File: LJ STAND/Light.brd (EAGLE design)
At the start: 112.3 x 112.3 mm, 182 parts

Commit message: Light PCB routing
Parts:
- moved C19 4.65 mm to (55.1, 17.6), flipped to the bottom, turned to 180 degrees
- moved C17 4.47 mm to (68.4, 19.7), flipped to the bottom, turned to 160 degrees
- moved C18 4.41 mm to (61.7, 18.0), flipped to the bottom, turned to 170 degrees
- moved C21 4.19 mm to (42.3, 20.1), flipped to the bottom, turned to 200 degrees
- moved C6 4.15 mm to (94.6, 55.0), flipped to the bottom, turned to 90 degrees
- moved C13 4.12 mm to (57.3, 94.7), turned to 0 degrees
- moved C9 3.97 mm to (89.1, 36.2), flipped to the bottom, turned to 120 degrees
- moved C22 3.97 mm to (36.2, 23.2), flipped to the bottom, turned to 210 degrees
- moved C8 3.90 mm to (92.1, 42.2), flipped to the bottom, turned to 110 degrees
- moved R27 3.89 mm to (60.6, 91.9), turned to 280 degrees
- moved C20 3.89 mm to (48.6, 18.6), flipped to the bottom, turned to 190 degrees
- moved C10 3.87 mm to (85.1, 30.6), flipped to the bottom, turned to 130 degrees
- moved C14 3.86 mm to (63.8, 94.0), turned to 10 degrees
- moved C25 3.84 mm to (22.4, 37.7), flipped to the bottom, turned to 240 degrees
- moved R25 3.82 mm to (54.2, 92.1), turned to 270 degrees
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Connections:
- removed net N$43: U$1.6
- removed net N$44: U$1.5
- removed net N$45: U$1.4
- removed net N$46: U$1.3
- removed net N$47: U$1.2
- removed net N$48: U$1.1
- removed net N$49: U$1.48
- removed net N$50: U$1.47
- removed net N$51: U$1.46
- removed net N$52: U$1.45
- removed net N$57: U$1.40
- removed net N$58: U$1.39
- removed net N$59: U$1.38
- removed net N$60: U$1.37
- removed net N$61: U$1.36
- removed net N$62: U$1.35
- removed net N$63: U$1.34
- removed net N$64: U$1.33
- removed net N$65: U$1.32
- removed net N$66: U$1.31
- removed net N$67: U$1.30
- removed net N$68: U$1.29
- removed net N$69: U$1.28
- removed net N$70: U$1.27
- removed net N$71: U$1.26
- removed net N$72: U$1.25
- net LS10: now also U$1.6
- net LS11: now also U$1.5
- net LS12: now also U$1.4
- net LS13: now also U$1.3
- net LS14: now also U$1.2
- net LS15: now also U$1.1
- net LS16: now also U$1.48
- net LS17: now also U$1.47
- net LS18: now also U$1.46
- net LS19: now also U$1.45
- net LS20: now also U$1.25
- net LS21: now also U$1.26
- net LS22: now also U$1.27
- net LS23: now also U$1.28
- net LS24: now also U$1.29
- net LS25: now also U$1.30
- net LS26: now also U$1.31
- net LS27: now also U$1.32
- net LS28: now also U$1.33
- net LS29: now also U$1.34
- net LS30: now also U$1.35
- net LS31: now also U$1.36
- net LS32: now also U$1.37
- net LS33: now also U$1.38
- net LS34: now also U$1.39
- net LS35: now also U$1.40
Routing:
- net 3.3V: track 0.00 -> 299.4 mm, vias 0 -> 34
- net LS33: track 0.00 -> 7.18 mm
- net LS19: track 0.00 -> 7.03 mm
- net LS20: track 0.00 -> 7.02 mm
- net LS15: track 0.00 -> 7.00 mm
- net LS23: track 0.00 -> 6.97 mm
- net LS1: track 0.00 -> 6.93 mm
- net LS21: track 0.00 -> 6.88 mm
- net LS18: track 0.00 -> 6.83 mm
- net LS24: track 0.00 -> 6.81 mm
- net LS27: track 0.00 -> 6.80 mm
- net LS29: track 0.00 -> 6.76 mm
- net LS28: track 0.00 -> 6.71 mm
- net LS6: track 0.00 -> 6.70 mm
- net LS2: track 0.00 -> 6.65 mm
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- added copper zone on layer 1, net 3.3V

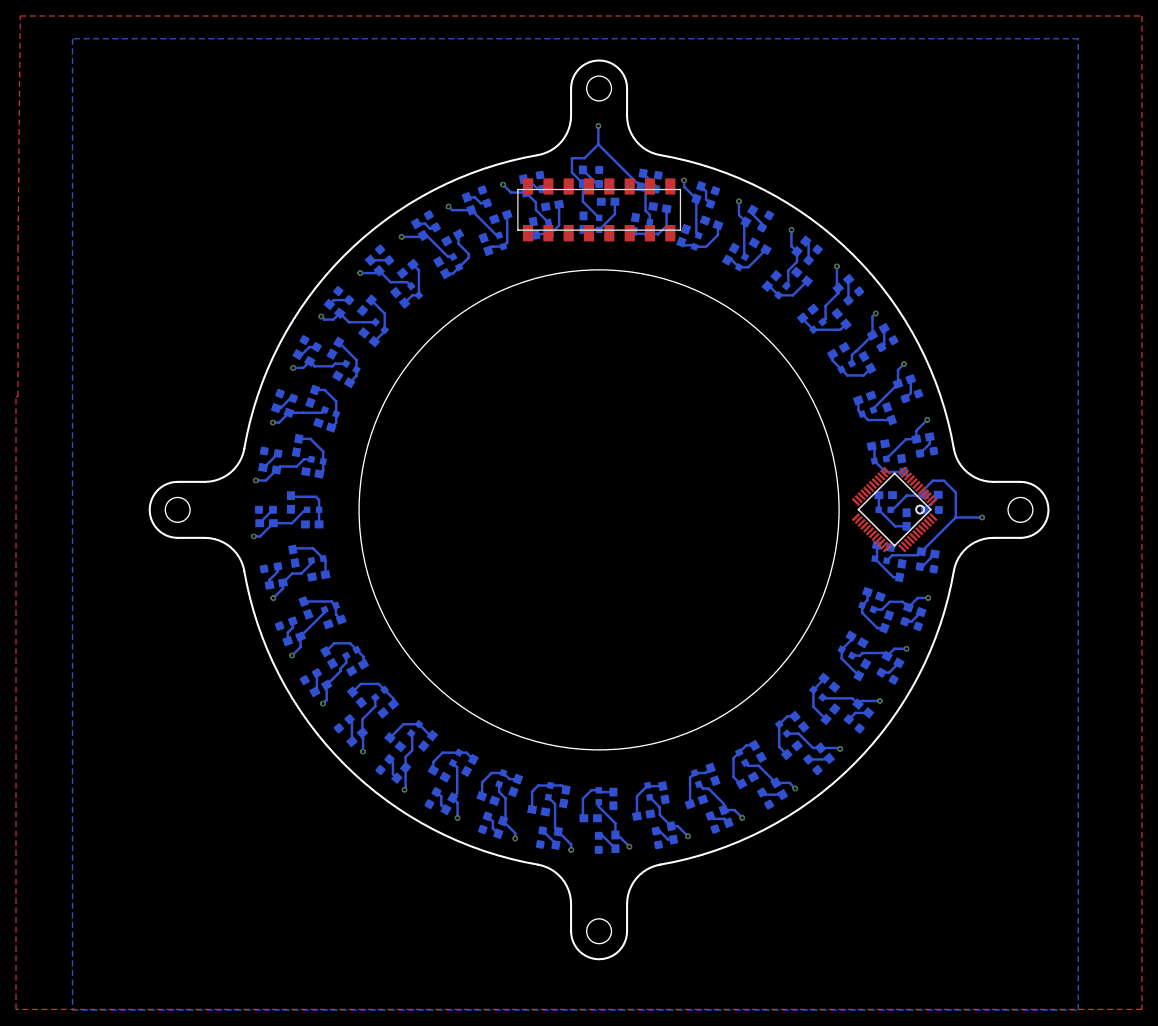
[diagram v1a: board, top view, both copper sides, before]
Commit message: Finished routing light & encoder pcbs
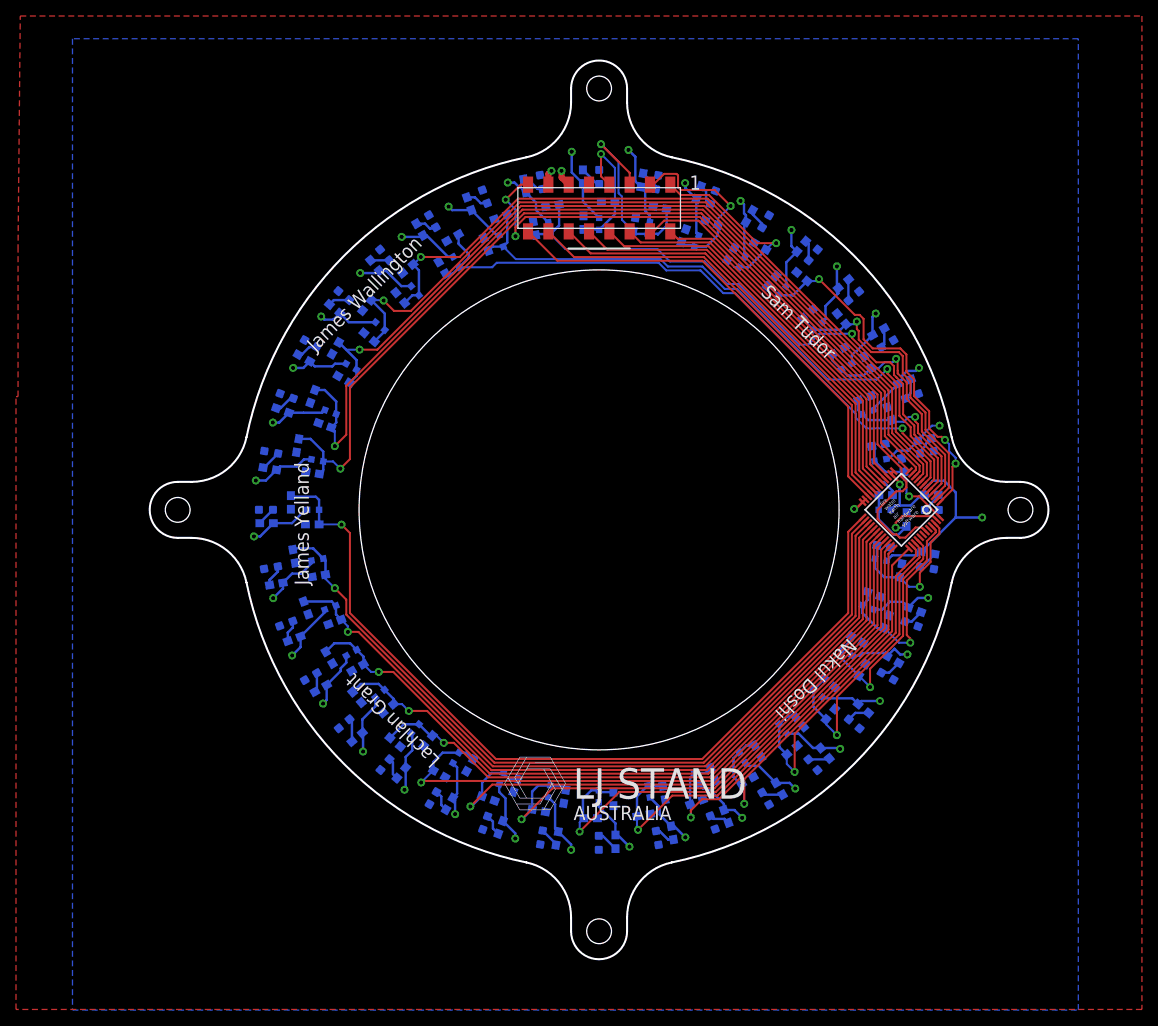
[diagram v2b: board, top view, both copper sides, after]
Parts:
- moved U$1 0.84 mm to (94.0, 56.2)
- moved R18 0.27 mm to (96.8, 64.9)
- moved JP1 0.23 mm to (56.2, 93.9)
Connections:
- net 3.3V: now also JP1.9; no longer JP1.1
- net A0: now also JP1.4; no longer JP1.7
- net A1: now also JP1.2; no longer JP1.8
- net A2: now also JP1.6; no longer JP1.9
- net A3: now also JP1.8; no longer JP1.10
- net A4: now also JP1.10; no longer JP1.11
- net EN: now also JP1.16; no longer JP1.13
- net GND: now also JP1.11, JP1.13; no longer JP1.14, JP1.16
- net LS0: now also JP1.7; no longer JP1.2
- net LS1: now also JP1.5; no longer JP1.3
- net LS10: now also U$1.46; no longer U$1.6
- net LS11: now also U$1.45; no longer U$1.5
- net LS12: now also U$1.40; no longer U$1.4
- net LS13: now also U$1.39; no longer U$1.3
- net LS14: now also U$1.38; no longer U$1.2
- net LS15: now also U$1.37; no longer U$1.1
- net LS16: now also U$1.36; no longer U$1.48
- net LS17: now also U$1.35; no longer U$1.47
- net LS18: now also U$1.34; no longer U$1.46
- net LS19: now also U$1.33; no longer U$1.45
- net LS2: now also JP1.3; no longer JP1.4
- net LS20: now also U$1.32; no longer U$1.25
- net LS21: now also U$1.31; no longer U$1.26
- net LS22: now also U$1.30; no longer U$1.27
- net LS23: now also U$1.29; no longer U$1.28
- net LS24: now also U$1.28; no longer U$1.29
- net LS25: now also U$1.27; no longer U$1.30
- net LS26: now also U$1.26; no longer U$1.31
- net LS27: now also U$1.25; no longer U$1.32
- net LS28: now also U$1.12; no longer U$1.33
- net LS29: now also U$1.11; no longer U$1.34
- net LS3: now also JP1.1; no longer JP1.5
- net LS30: now also U$1.10; no longer U$1.35
- net LS31: now also U$1.9; no longer U$1.36
- net LS32: now also U$1.8; no longer U$1.37
- net LS33: now also U$1.7; no longer U$1.38
- net LS34: now also U$1.6; no longer U$1.39
- net LS35: now also U$1.5; no longer U$1.40
- net LS4: now also U$1.1; no longer U$1.12
- net LS5: now also U$1.2; no longer U$1.11
- net LS6: now also U$1.3; no longer U$1.10
- net LS7: now also U$1.4; no longer U$1.9
- net LS8: now also U$1.48; no longer U$1.8
- net LS9: now also U$1.47; no longer U$1.7
- net MUX_OUT: now also JP1.15; no longer JP1.6
- net WR: now also JP1.14; no longer JP1.15
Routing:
- net LS28: track 6.71 -> 115.8 mm, vias 0 -> 1
- net LS29: track 6.76 -> 115.4 mm, vias 0 -> 1
- net LS27: track 6.80 -> 111.2 mm, vias 0 -> 1
- net LS30: track 6.31 -> 105.1 mm, vias 0 -> 1
- net LS26: track 6.54 -> 103.6 mm, vias 0 -> 1
- net LS31: track 6.42 -> 100.6 mm, vias 0 -> 1
- net LS25: track 6.27 -> 98.6 mm, vias 0 -> 1
- net MUX_OUT: track 0.00 -> 91.5 mm, vias 0 -> 2
- net LS24: track 6.81 -> 94.2 mm, vias 0 -> 1
- net LS32: track 6.36 -> 93.7 mm, vias 0 -> 1
- net LS23: track 6.97 -> 89.1 mm, vias 0 -> 1
- net LS21: track 6.88 -> 84.9 mm, vias 0 -> 1
- net LS22: track 6.61 -> 82.8 mm, vias 0 -> 1
- net LS33: track 7.18 -> 80.6 mm, vias 0 -> 1
- net LS34: track 6.28 -> 79.4 mm, vias 0 -> 1
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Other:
- outline, holes or cut-outs redrawn
- board text added: "1"
- board text added: "AUSTRALIA"
- board text added: "James Wallington"
- board text added: "James Yelland"
- board text added: "LJ STAND"
- board text added: "Lachlan Grant"
- board text added: "Nakul Doshi"
- board text added: "Sam Tudor"
- board text added: "fire water earth air hardware software"

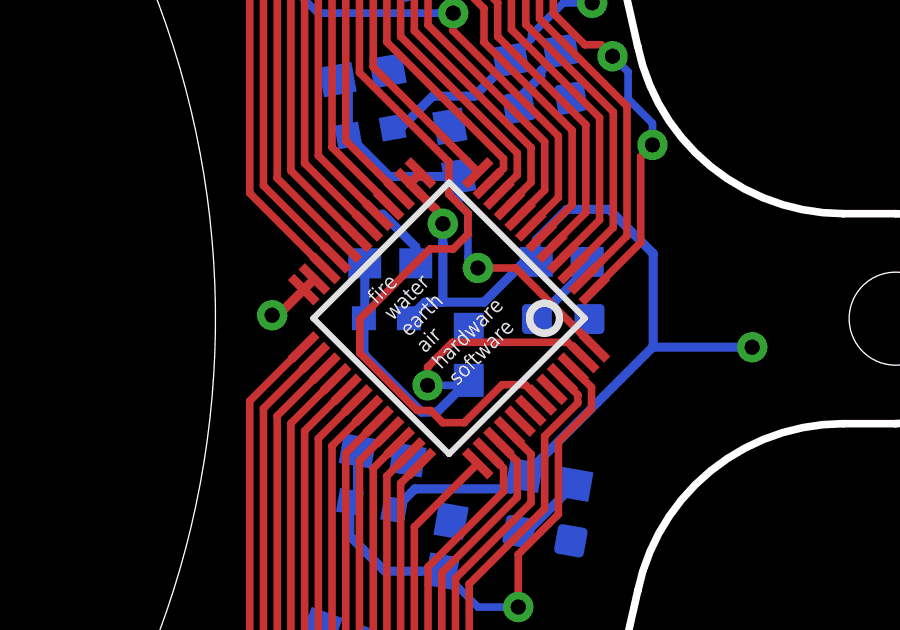
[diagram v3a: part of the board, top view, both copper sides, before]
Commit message: Finalisation of gyro, encoder and light boards + gerbers, silkscreen fixes
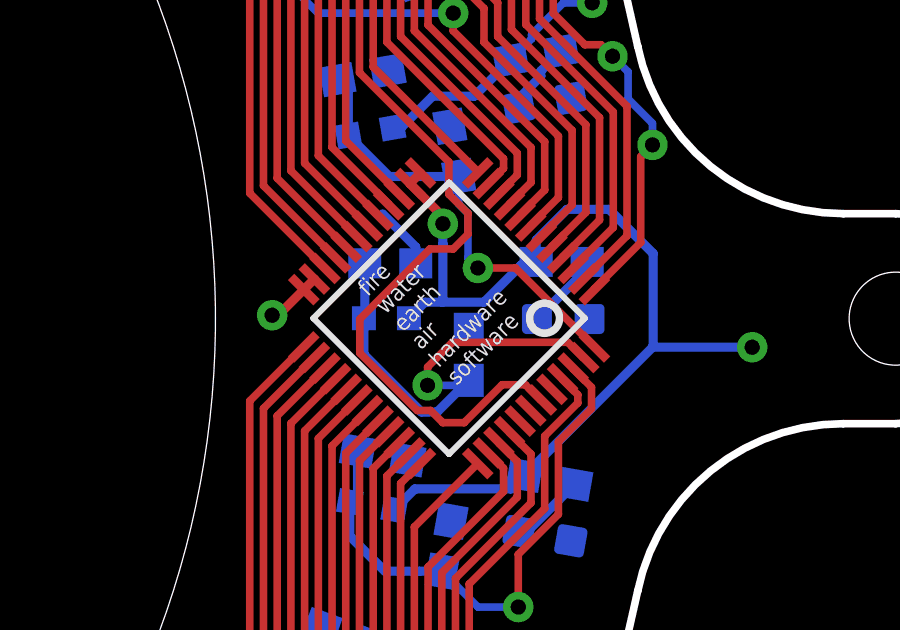
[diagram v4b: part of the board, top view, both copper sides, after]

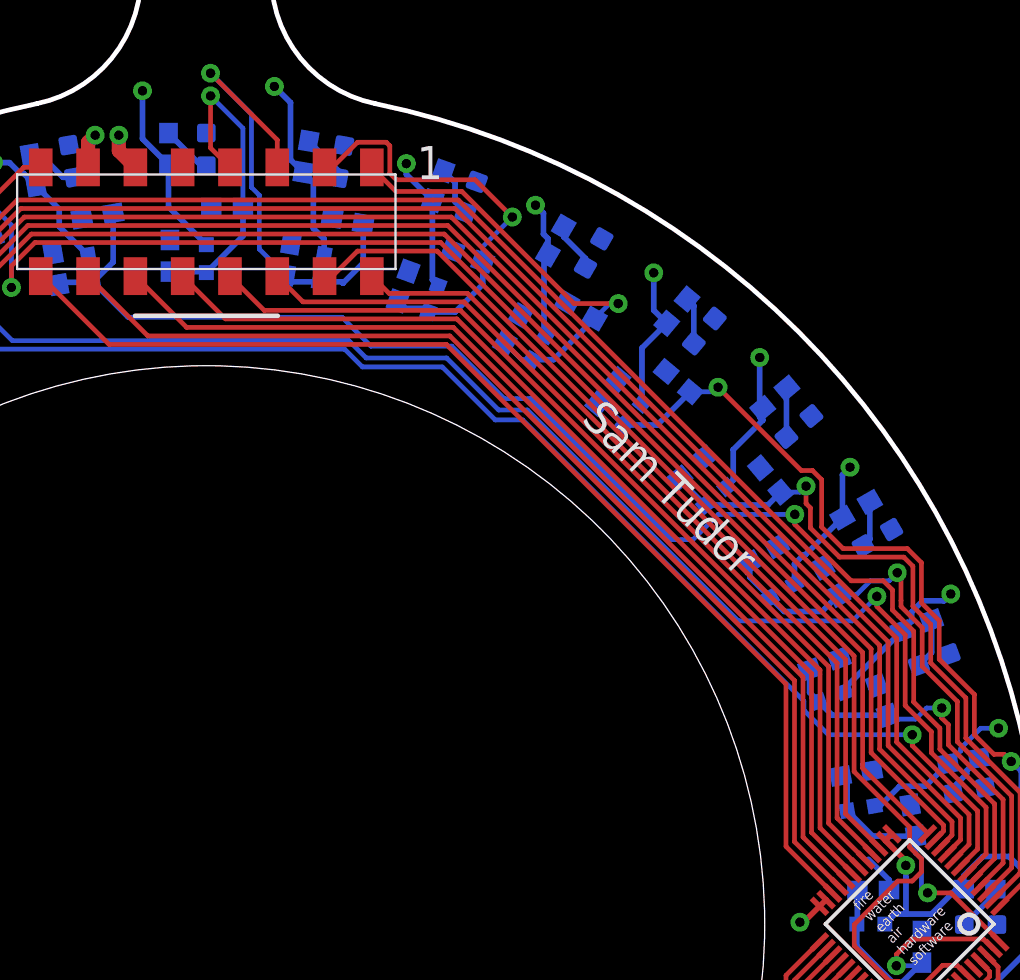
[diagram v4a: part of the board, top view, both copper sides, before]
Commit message: Pin changes on teensys, removed some screen pins for motor grounding
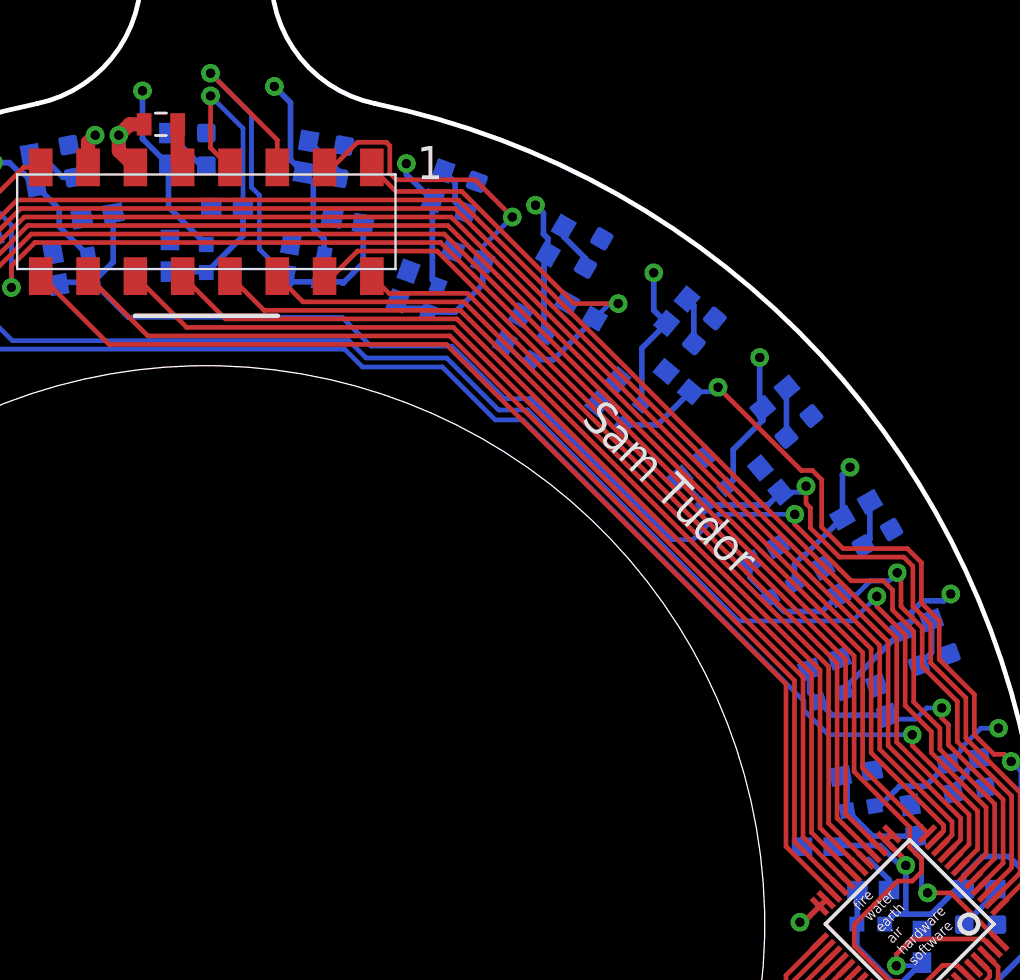
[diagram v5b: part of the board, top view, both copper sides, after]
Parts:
- added C37: 0.1uF, SparkFun-Capacitors:0603-CAP
- added C38: 10uF, SparkFun-Capacitors:0805
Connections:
- net 3.3V: now also C37.2, C38.1
- net GND: now also C37.1, C38.2
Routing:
- net 3.3V: track 297.4 -> 304.2 mm
- net GND: track 8.00 -> 9.60 mm
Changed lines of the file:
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@@
 <layer number="27" name="tValues" color="7" fill="1" visible="yes" active="yes"/>
 <layer number="28" name="bValues" color="7" fill="1" visible="yes" active="yes"/>
-<layer number="29" name="tStop" color="7" fill="3" visible="no" active="yes"/>
-<layer number="30" name="bStop" color="7" fill="6" visible="no" active="yes"/>
+<layer number="29" name="tStop" color="7" fill="3" visible="yes" active="yes"/>
+<layer number="30" name="bStop" color="7" fill="6" visible="yes" active="yes"/>
 <layer number="31" name="tCream" color="7" fill="4" visible="no" active="yes"/>
 <layer number="32" name="bCream" color="7" fill="5" visible="no" active="yes"/>
@@
 </element>
 <element name="U$1" library="analog-devices" library_urn="urn:adsk.eagle:library:2033836" package="QFP-7X7-48-NO-EXP" package3d_urn="urn:adsk.eagle:package:2034172/2" value="ADG732" x="93.960090625" y="56.185471875" smashed="yes" rot="R135"/>
+<element name="C37" library="SparkFun-Capacitors" package="0603-CAP" value="0.1uF" x="89.027" y="60.3504" smashed="yes" rot="MR180">
+<attribute name="VALUE" x="86.2838" y="62.1538" size="1.016" layer="28" font="vector" rot="MR180"/>
+</element>
+<element name="C38" library="SparkFun-Capacitors" package="0805" value="10uF" x="53.7464" y="99.1362" smashed="yes" rot="R180">
+<attribute name="VALUE" x="54.0512" y="103.5812" size="1.016" layer="27" font="vector" rot="R270"/>
+</element>
 </elements>
 <signals>
@@
 <wire x1="49.8348" y1="98.171" x2="50.2158" y2="98.552" width="0.762" layer="1"/>
 <via x="50.2158" y="98.552" extent="1-16" drill="0.508"/>
+<contactref element="C37" pad="1"/>
+<contactref element="C38" pad="2"/>
+<wire x1="52.8464" y1="99.1362" x2="52.07" y2="99.1362" width="0.762" layer="1"/>
+<wire x1="52.07" y1="99.1362" x2="51.4858" y2="98.552" width="0.762" layer="1"/>
 </signal>
 <signal name="N$2">
@@
 <wire x1="95.7956" y1="73.5452" x2="96.1644" y2="73.914" width="0.3048" layer="16"/>
 <via x="96.1644" y="73.914" extent="1-16" drill="0.508"/>
+<contactref element="C37" pad="2"/>
+<wire x1="93.7514" y1="59.3344" x2="93.4466" y2="59.3344" width="0.3048" layer="16"/>
+<wire x1="93.4466" y1="59.3344" x2="92.378765625" y2="60.402234375" width="0.3048" layer="16"/>
+<wire x1="92.378765625" y1="60.402234375" x2="92.12575625" y2="60.402278125" width="0.3048" layer="16"/>
+<wire x1="92.12575625" y1="60.402278125" x2="89.928878125" y2="60.402278125" width="0.3048" layer="16"/>
+<wire x1="89.928878125" y1="60.402278125" x2="89.877" y2="60.3504" width="0.3048" layer="16"/>
+<contactref element="C38" pad="1"/>
+<wire x1="54.6464" y1="99.1362" x2="54.6464" y2="97.0936" width="0.762" layer="1"/>
+<wire x1="54.6464" y1="97.0936" x2="54.9148" y2="96.8252" width="0.762" layer="1"/>
 </signal>
 <signal name="N$1">
